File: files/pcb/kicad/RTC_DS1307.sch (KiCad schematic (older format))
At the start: 0 parts

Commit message: 回路図更新
温度湿度センサ
大気圧センサ
輝度センサ
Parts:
- added C?: 5.5V 0.1F, ~, symbol CP1
- added D?: DIODE, ~, symbol DIODE
- added IC?: DS1307, symbol IC_8PIN
- added R?: 100k, ~, symbol R
- added R?: 10k, ~, symbol R
- added X?: CRYSTAL, ~, symbol CRYSTAL
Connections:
- new net: IC?.1, X?.2
- new net: IC?.2, X?.1
- new net: C?.1, IC?.3, R?.2
- new net: D?.2 (K), R?.1
- new net +5V: D?.1 (A), IC?.8, R?.1
- new net CLKOUT: IC?.7, R?.2
- new net GND: C?.2, IC?.4
- new net SCL: IC?.6
- new net SDA: IC?.5
- no-connect marks 0 -> 1
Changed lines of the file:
@@
 $Descr A4 11693 8268
 encoding utf-8
-Sheet 1 12
+Sheet 10 12
 Title ""
 Date "23 aug 2014"
@@
 Comment4 ""
 $EndDescr
+Text HLabel 7200 4200 2    39   Input ~ 0
+SCL
+Text HLabel 7200 4300 2    39   Input ~ 0
+SDA
+Text HLabel 7200 4000 2    39   Input ~ 0
+CLKEN
+Text HLabel 7200 4100 2    39   Input ~ 0
+CLKOUT
+$Comp
+L IC_8PIN IC?
+U 1 1 53F95FB5
+P 6100 4150
+F 0 "IC?" H 6100 4400 39  0000 C CNN
+F 1 "DS1307" H 6100 4150 39  0000 C CNN
+F 2 "" H 6100 4050 60  0000 C CNN
+F 3 "" H 6100 4050 60  0000 C CNN
+	1    6100 4150
+	1    0    0    -1
+$EndComp
+$Comp
+L CRYSTAL X?
+U 1 1 53F95FD5
+P 5200 3850
+F 0 "X?" H 5200 4000 60  0000 C CNN
+F 1 "CRYSTAL" H 5200 3700 60  0000 C CNN
+F 2 "~" H 5200 3850 60  0000 C CNN
+F 3 "~" H 5200 3850 60  0000 C CNN
+	1    5200 3850
+	1    0    0    -1
+$EndComp
+$Comp
+L CP1 C?
+U 1 1 53F95FE8
+P 4550 4450
+F 0 "C?" H 4600 4550 50  0000 L CNN
+F 1 "5.5V 0.1F" H 4600 4350 50  0000 L CNN
+F 2 "~" H 4550 4450 60  0000 C CNN
+F 3 "~" H 4550 4450 60  0000 C CNN
+	1    4550 4450
+	1    0    0    -1
+$EndComp
+$Comp
+L DIODE D?
+U 1 1 53F95FF7
+P 4550 3400
+F 0 "D?" H 4550 3500 40  0000 C CNN
+F 1 "DIODE" H 4550 3300 40  0000 C CNN
+F 2 "~" H 4550 3400 60  0000 C CNN
+F 3 "~" H 4550 3400 60  0000 C CNN
+	1    4550 3400
+	0    1    1    0
+$EndComp
+$Comp
+L R R?
+U 1 1 53F96006
+P 4550 3900
+F 0 "R?" V 4630 3900 40  0000 C CNN
+F 1 "100k" V 4557 3901 40  0000 C CNN
+F 2 "~" V 4480 3900 30  0000 C CNN
+F 3 "~" H 4550 3900 30  0000 C CNN
+	1    4550 3900
+	1    0    0    -1
+$EndComp
+$Comp
+L +5V #PWR?
+U 1 1 53F9602E
+P 4550 3150
+F 0 "#PWR?" H 4550 3240 20  0001 C CNN
+F 1 "+5V" H 4550 3240 30  0000 C CNN
+F 2 "" H 4550 3150 60  0000 C CNN
+F 3 "" H 4550 3150 60  0000 C CNN
+	1    4550 3150
+	1    0    0    -1
+$EndComp
+$Comp
+L GND #PWR?
+U 1 1 53F96055
+P 4550 4750
+F 0 "#PWR?" H 4550 4750 30  0001 C CNN
+F 1 "GND" H 4550 4680 30  0001 C CNN
+F 2 "" H 4550 4750 60  0000 C CNN
+F 3 "" H 4550 4750 60  0000 C CNN
+	1    4550 4750
+	1    0    0    -1
+$EndComp
+Wire Wire Line
+	5650 4000 5500 4000
+Wire Wire Line
+	5650 4100 4900 4100
+Wire Wire Line
+	4900 4100 4900 3850
+Wire Wire Line
+	4550 3150 4550 3200
+Wire Wire Line
+	4550 3600 4550 3650
+Wire Wire Line
+	4550 4150 4550 4200
+Wire Wire Line
+	4550 4200 4550 4250
+Wire Wire Line
+	4550 4650 4550 4750
+Wire Wire Line
+	6700 4000 6550 4000
+Wire Wire Line
+	6700 3400 6700 4000
+Connection ~ 4550 4200
+Wire Wire Line
+	6550 4100 6950 4100
+Wire Wire Line
+	6950 4100 7200 4100
+Wire Wire Line
+	6950 4000 6950 4100
+$Comp
+L R R?
+U 1 1 53F960B9
+P 6950 3750
+F 0 "R?" V 7030 3750 40  0000 C CNN
+F 1 "10k" V 6957 3751 40  0000 C CNN
+F 2 "~" V 6880 3750 30  0000 C CNN
+F 3 "~" H 6950 3750 30  0000 C CNN
+	1    6950 3750
+	1    0    0    -1
+$EndComp
+Connection ~ 6950 4100
+Wire Wire Line
+	6550 4200 7200 4200
+Wire Wire Line
+	6550 4300 7200 4300
+NoConn ~ 7200 4000
+Wire Wire Line
+	5650 4200 4550 4200
+$Comp
+L +5V #PWR?
+U 1 1 53F961EF
+P 6700 3400
+F 0 "#PWR?" H 6700 3490 20  0001 C CNN
+F 1 "+5V" H 6700 3490 30  0000 C CNN
+F 2 "" H 6700 3400 60  0000 C CNN
+F 3 "" H 6700 3400 60  0000 C CNN
+	1    6700 3400
+	1    0    0    -1
+$EndComp
+$Comp
+L GND #PWR?
+U 1 1 53F961FF
+P 5500 4450
+F 0 "#PWR?" H 5500 4450 30  0001 C CNN
+F 1 "GND" H 5500 4380 30  0001 C CNN
+F 2 "" H 5500 4450 60  0000 C CNN
+F 3 "" H 5500 4450 60  0000 C CNN
+	1    5500 4450
+	1    0    0    -1
+$EndComp
+Wire Wire Line
+	5650 4300 5500 4300
+Wire Wire Line
+	5500 4300 5500 4450
+Wire Wire Line
+	6950 3400 6950 3500
+$Comp
+L +5V #PWR?
+U 1 1 53F96268
+P 6950 3400
+F 0 "#PWR?" H 6950 3490 20  0001 C CNN
+F 1 "+5V" H 6950 3490 30  0000 C CNN
+F 2 "" H 6950 3400 60  0000 C CNN
+F 3 "" H 6950 3400 60  0000 C CNN
+	1    6950 3400
+	1    0    0    -1
+$EndComp
+Wire Wire Line
+	5500 4000 5500 3850
 $EndSCHEMATC

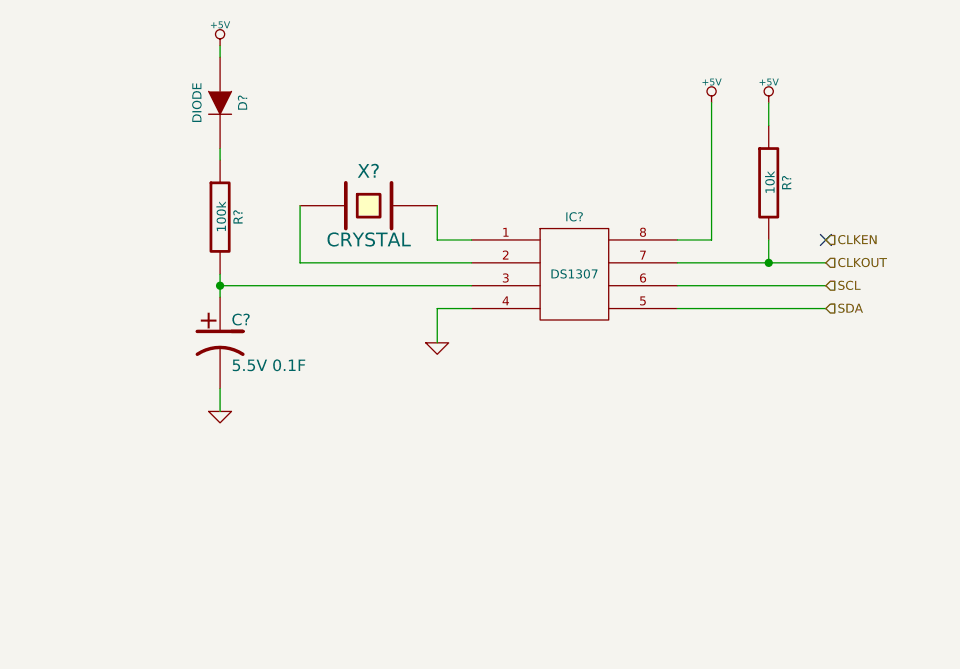
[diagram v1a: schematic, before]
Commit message: 回路図更新、DS1307対応
バスの接続が未
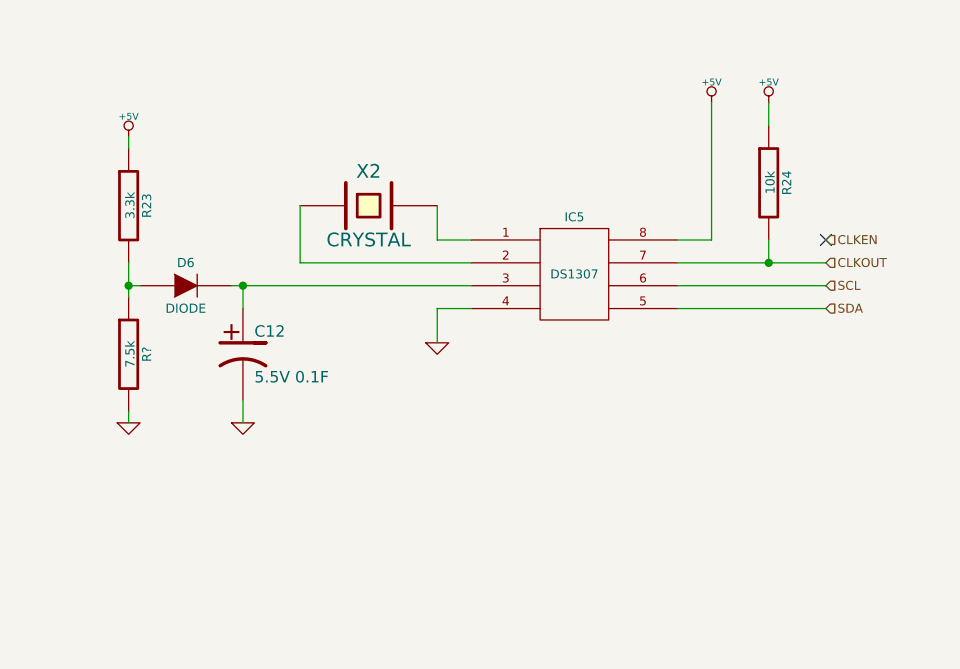
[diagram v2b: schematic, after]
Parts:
- added R?: 7.5k, ~, symbol R
- R23: renamed from R?; value 100k -> 3.3k
- gave numbers to parts that had none: 5
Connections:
- net +5V: now also R23.1; no longer D6.1 (A)
- net GND: now also R?.2
- net at C12.1, IC5.3: now also D6.2 (K); no longer R23.2
- new net: D6.1 (A), R23.2, R?.1
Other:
- moved on the sheet: C12, D6, R23
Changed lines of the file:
@@
 $Descr A4 11693 8268
 encoding utf-8
-Sheet 10 12
+Sheet 11 13
 Title ""
-Date "23 aug 2014"
+Date "24 aug 2014"
 Rev ""
 Comp ""
@@
 CLKOUT
 $Comp
-L IC_8PIN IC?
+L IC_8PIN IC5
 U 1 1 53F95FB5
 P 6100 4150
-F 0 "IC?" H 6100 4400 39  0000 C CNN
+F 0 "IC5" H 6100 4400 39  0000 C CNN
 F 1 "DS1307" H 6100 4150 39  0000 C CNN
 F 2 "" H 6100 4050 60  0000 C CNN
@@
 $EndComp
 $Comp
-L CRYSTAL X?
+L CRYSTAL X2
 U 1 1 53F95FD5
 P 5200 3850
-F 0 "X?" H 5200 4000 60  0000 C CNN
+F 0 "X2" H 5200 4000 60  0000 C CNN
 F 1 "CRYSTAL" H 5200 3700 60  0000 C CNN
 F 2 "~" H 5200 3850 60  0000 C CNN
@@
 $EndComp
 $Comp
-L CP1 C?
+L CP1 C12
 U 1 1 53F95FE8
-P 4550 4450
-F 0 "C?" H 4600 4550 50  0000 L CNN
-F 1 "5.5V 0.1F" H 4600 4350 50  0000 L CNN
-F 2 "~" H 4550 4450 60  0000 C CNN
-F 3 "~" H 4550 4450 60  0000 C CNN
-	1    4550 4450
-	1    0    0    -1
-$EndComp
-$Comp
-L DIODE D?
+P 4650 4500
+F 0 "C12" H 4700 4600 50  0000 L CNN
+F 1 "5.5V 0.1F" H 4700 4400 50  0000 L CNN
+F 2 "~" H 4650 4500 60  0000 C CNN
+F 3 "~" H 4650 4500 60  0000 C CNN
+	1    4650 4500
+	1    0    0    -1
+$EndComp
+$Comp
+L DIODE D6
 U 1 1 53F95FF7
-P 4550 3400
-F 0 "D?" H 4550 3500 40  0000 C CNN
-F 1 "DIODE" H 4550 3300 40  0000 C CNN
-F 2 "~" H 4550 3400 60  0000 C CNN
-F 3 "~" H 4550 3400 60  0000 C CNN
-	1    4550 3400
-	0    1    1    0
-$EndComp
-$Comp
-L R R?
+P 4400 4200
+F 0 "D6" H 4400 4300 40  0000 C CNN
+F 1 "DIODE" H 4400 4100 40  0000 C CNN
+F 2 "~" H 4400 4200 60  0000 C CNN
+F 3 "~" H 4400 4200 60  0000 C CNN
+	1    4400 4200
+	1    0    0    -1
+$EndComp
+$Comp
+L R R23
 U 1 1 53F96006
-P 4550 3900
-F 0 "R?" V 4630 3900 40  0000 C CNN
-F 1 "100k" V 4557 3901 40  0000 C CNN
-F 2 "~" V 4480 3900 30  0000 C CNN
-F 3 "~" H 4550 3900 30  0000 C CNN
-	1    4550 3900
-	1    0    0    -1
-$EndComp
-$Comp
-L +5V #PWR?
+P 4150 3850
+F 0 "R23" V 4230 3850 40  0000 C CNN
+F 1 "3.3k" V 4157 3851 40  0000 C CNN
+F 2 "~" V 4080 3850 30  0000 C CNN
+F 3 "~" H 4150 3850 30  0000 C CNN
+	1    4150 3850
+	1    0    0    -1
+$EndComp
+$Comp
+L +5V #PWR49
 U 1 1 53F9602E
-P 4550 3150
-F 0 "#PWR?" H 4550 3240 20  0001 C CNN
-F 1 "+5V" H 4550 3240 30  0000 C CNN
-F 2 "" H 4550 3150 60  0000 C CNN
-F 3 "" H 4550 3150 60  0000 C CNN
-	1    4550 3150
-	1    0    0    -1
-$EndComp
-$Comp
-L GND #PWR?
+P 4150 3550
+F 0 "#PWR49" H 4150 3640 20  0001 C CNN
+F 1 "+5V" H 4150 3640 30  0000 C CNN
+F 2 "" H 4150 3550 60  0000 C CNN
+F 3 "" H 4150 3550 60  0000 C CNN
+	1    4150 3550
+	1    0    0    -1
+$EndComp
+$Comp
+L GND #PWR50
 U 1 1 53F96055
-P 4550 4750
-F 0 "#PWR?" H 4550 4750 30  0001 C CNN
-F 1 "GND" H 4550 4680 30  0001 C CNN
-F 2 "" H 4550 4750 60  0000 C CNN
-F 3 "" H 4550 4750 60  0000 C CNN
-	1    4550 4750
+P 4150 4800
+F 0 "#PWR50" H 4150 4800 30  0001 C CNN
+F 1 "GND" H 4150 4730 30  0001 C CNN
+F 2 "" H 4150 4800 60  0000 C CNN
+F 3 "" H 4150 4800 60  0000 C CNN
+	1    4150 4800
 	1    0    0    -1
 $EndComp
@@
 	4900 4100 4900 3850
 Wire Wire Line
-	4550 3150 4550 3200
-Wire Wire Line
-	4550 3600 4550 3650
-Wire Wire Line
-	4550 4150 4550 4200
-Wire Wire Line
-	4550 4200 4550 4250
-Wire Wire Line
-	4550 4650 4550 4750
+	4150 3550 4150 3600
+Wire Wire Line
+	4150 4750 4150 4800
 Wire Wire Line
 	6700 4000 6550 4000
 Wire Wire Line
 	6700 3400 6700 4000
-Connection ~ 4550 4200
 Wire Wire Line
 	6550 4100 6950 4100
@@
 	6950 4000 6950 4100
 $Comp
-L R R?
+L R R24
 U 1 1 53F960B9
 P 6950 3750
-F 0 "R?" V 7030 3750 40  0000 C CNN
+F 0 "R24" V 7030 3750 40  0000 C CNN
 F 1 "10k" V 6957 3751 40  0000 C CNN
 F 2 "~" V 6880 3750 30  0000 C CNN
@@
 	6550 4300 7200 4300
 NoConn ~ 7200 4000
-Wire Wire Line
-	5650 4200 4550 4200
-$Comp
-L +5V #PWR?
+$Comp
+L +5V #PWR52
 U 1 1 53F961EF
 P 6700 3400
-F 0 "#PWR?" H 6700 3490 20  0001 C CNN
+F 0 "#PWR52" H 6700 3490 20  0001 C CNN
 F 1 "+5V" H 6700 3490 30  0000 C CNN
 F 2 "" H 6700 3400 60  0000 C CNN
@@
 $EndComp
 $Comp
-L GND #PWR?
+L GND #PWR51
 U 1 1 53F961FF
 P 5500 4450
-F 0 "#PWR?" H 5500 4450 30  0001 C CNN
+F 0 "#PWR51" H 5500 4450 30  0001 C CNN
 F 1 "GND" H 5500 4380 30  0001 C CNN
 F 2 "" H 5500 4450 60  0000 C CNN
@@
 	6950 3400 6950 3500
 $Comp
-L +5V #PWR?
+L +5V #PWR53
 U 1 1 53F96268
 P 6950 3400
-F 0 "#PWR?" H 6950 3490 20  0001 C CNN
+F 0 "#PWR53" H 6950 3490 20  0001 C CNN
 F 1 "+5V" H 6950 3490 30  0000 C CNN
 F 2 "" H 6950 3400 60  0000 C CNN
@@
 Wire Wire Line
 	5500 4000 5500 3850
+$Comp
+L R R?
+U 1 1 53FA233E
+P 4150 4500
+F 0 "R?" V 4230 4500 40  0000 C CNN
+F 1 "7.5k" V 4157 4501 40  0000 C CNN
+F 2 "~" V 4080 4500 30  0000 C CNN
+F 3 "~" H 4150 4500 30  0000 C CNN
+	1    4150 4500
+	1    0    0    -1
+$EndComp
+Wire Wire Line
+	4150 4100 4150 4200
+Wire Wire Line
+	4150 4200 4150 4250
+Wire Wire Line
+	4200 4200 4150 4200
+Connection ~ 4150 4200
+$Comp
+L GND #PWR?
+U 1 1 53FA2AE8
+P 4650 4800
+F 0 "#PWR?" H 4650 4800 30  0001 C CNN
+F 1 "GND" H 4650 4730 30  0001 C CNN
+F 2 "" H 4650 4800 60  0000 C CNN
+F 3 "" H 4650 4800 60  0000 C CNN
+	1    4650 4800
+	1    0    0    -1
+$EndComp
+Wire Wire Line
+	4650 4700 4650 4800
+Wire Wire Line
+	4650 4200 4650 4300
+Connection ~ 4650 4200
+Wire Wire Line
+	4600 4200 4650 4200
+Wire Wire Line
+	4650 4200 5650 4200
 $EndSCHEMATC

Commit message: 回路図ERC途中
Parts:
- gave numbers to parts that had none: 1
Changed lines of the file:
@@
 Sheet 11 13
 Title ""
-Date "24 aug 2014"
+Date "25 aug 2014"
 Rev ""
 Comp ""
@@
 $EndComp
 $Comp
-L +5V #PWR49
+L +5V #PWR051
 U 1 1 53F9602E
 P 4150 3550
-F 0 "#PWR49" H 4150 3640 20  0001 C CNN
+F 0 "#PWR051" H 4150 3640 20  0001 C CNN
 F 1 "+5V" H 4150 3640 30  0000 C CNN
 F 2 "" H 4150 3550 60  0000 C CNN
@@
 $EndComp
 $Comp
-L GND #PWR50
+L GND #PWR052
 U 1 1 53F96055
 P 4150 4800
-F 0 "#PWR50" H 4150 4800 30  0001 C CNN
+F 0 "#PWR052" H 4150 4800 30  0001 C CNN
 F 1 "GND" H 4150 4730 30  0001 C CNN
 F 2 "" H 4150 4800 60  0000 C CNN
@@
 	6700 3400 6700 4000
 Wire Wire Line
-	6550 4100 6950 4100
-Wire Wire Line
-	6950 4100 7200 4100
+	6550 4100 7200 4100
 Wire Wire Line
 	6950 4000 6950 4100
@@
 NoConn ~ 7200 4000
 $Comp
-L +5V #PWR52
+L +5V #PWR053
 U 1 1 53F961EF
 P 6700 3400
-F 0 "#PWR52" H 6700 3490 20  0001 C CNN
+F 0 "#PWR053" H 6700 3490 20  0001 C CNN
 F 1 "+5V" H 6700 3490 30  0000 C CNN
 F 2 "" H 6700 3400 60  0000 C CNN
@@
 $EndComp
 $Comp
-L GND #PWR51
+L GND #PWR054
 U 1 1 53F961FF
 P 5500 4450
-F 0 "#PWR51" H 5500 4450 30  0001 C CNN
+F 0 "#PWR054" H 5500 4450 30  0001 C CNN
 F 1 "GND" H 5500 4380 30  0001 C CNN
 F 2 "" H 5500 4450 60  0000 C CNN
@@
 	6950 3400 6950 3500
 $Comp
-L +5V #PWR53
+L +5V #PWR055
 U 1 1 53F96268
 P 6950 3400
-F 0 "#PWR53" H 6950 3490 20  0001 C CNN
+F 0 "#PWR055" H 6950 3490 20  0001 C CNN
 F 1 "+5V" H 6950 3490 30  0000 C CNN
 F 2 "" H 6950 3400 60  0000 C CNN
@@
 	5500 4000 5500 3850
 $Comp
-L R R?
+L R R29
 U 1 1 53FA233E
 P 4150 4500
-F 0 "R?" V 4230 4500 40  0000 C CNN
+F 0 "R29" V 4230 4500 40  0000 C CNN
 F 1 "7.5k" V 4157 4501 40  0000 C CNN
 F 2 "~" V 4080 4500 30  0000 C CNN
@@
 $EndComp
 Wire Wire Line
-	4150 4100 4150 4200
-Wire Wire Line
-	4150 4200 4150 4250
+	4150 4100 4150 4250
 Wire Wire Line
 	4200 4200 4150 4200
 Connection ~ 4150 4200
 $Comp
-L GND #PWR?
+L GND #PWR056
 U 1 1 53FA2AE8
 P 4650 4800
-F 0 "#PWR?" H 4650 4800 30  0001 C CNN
+F 0 "#PWR056" H 4650 4800 30  0001 C CNN
 F 1 "GND" H 4650 4730 30  0001 C CNN
 F 2 "" H 4650 4800 60  0000 C CNN
@@
 Connection ~ 4650 4200
 Wire Wire Line
-	4600 4200 4650 4200
-Wire Wire Line
-	4650 4200 5650 4200
+	4600 4200 5650 4200
 $EndSCHEMATC

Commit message: 回路図ERC完了
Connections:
- no-connect marks 1 -> 0
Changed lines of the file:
@@
 Sheet 11 13
 Title ""
-Date "25 aug 2014"
+Date "26 aug 2014"
 Rev ""
 Comp ""
@@
 Text HLabel 7200 4300 2    39   Input ~ 0
 SDA
-Text HLabel 7200 4000 2    39   Input ~ 0
-CLKEN
 Text HLabel 7200 4100 2    39   Input ~ 0
 CLKOUT
@@
 $EndComp
 $Comp
-L +5V #PWR051
+L +5V #PWR059
 U 1 1 53F9602E
 P 4150 3550
-F 0 "#PWR051" H 4150 3640 20  0001 C CNN
+F 0 "#PWR059" H 4150 3640 20  0001 C CNN
 F 1 "+5V" H 4150 3640 30  0000 C CNN
 F 2 "" H 4150 3550 60  0000 C CNN
@@
 $EndComp
 $Comp
-L GND #PWR052
+L GND #PWR060
 U 1 1 53F96055
 P 4150 4800
-F 0 "#PWR052" H 4150 4800 30  0001 C CNN
+F 0 "#PWR060" H 4150 4800 30  0001 C CNN
 F 1 "GND" H 4150 4730 30  0001 C CNN
 F 2 "" H 4150 4800 60  0000 C CNN
@@
 Wire Wire Line
 	6550 4300 7200 4300
-NoConn ~ 7200 4000
 $Comp
-L +5V #PWR053
+L +5V #PWR061
 U 1 1 53F961EF
 P 6700 3400
-F 0 "#PWR053" H 6700 3490 20  0001 C CNN
+F 0 "#PWR061" H 6700 3490 20  0001 C CNN
 F 1 "+5V" H 6700 3490 30  0000 C CNN
 F 2 "" H 6700 3400 60  0000 C CNN
@@
 $EndComp
 $Comp
-L GND #PWR054
+L GND #PWR062
 U 1 1 53F961FF
 P 5500 4450
-F 0 "#PWR054" H 5500 4450 30  0001 C CNN
+F 0 "#PWR062" H 5500 4450 30  0001 C CNN
 F 1 "GND" H 5500 4380 30  0001 C CNN
 F 2 "" H 5500 4450 60  0000 C CNN
@@
 	6950 3400 6950 3500
 $Comp
-L +5V #PWR055
+L +5V #PWR063
 U 1 1 53F96268
 P 6950 3400
-F 0 "#PWR055" H 6950 3490 20  0001 C CNN
+F 0 "#PWR063" H 6950 3490 20  0001 C CNN
 F 1 "+5V" H 6950 3490 30  0000 C CNN
 F 2 "" H 6950 3400 60  0000 C CNN
@@
 Connection ~ 4150 4200
 $Comp
-L GND #PWR056
+L GND #PWR064
 U 1 1 53FA2AE8
 P 4650 4800
-F 0 "#PWR056" H 4650 4800 30  0001 C CNN
+F 0 "#PWR064" H 4650 4800 30  0001 C CNN
 F 1 "GND" H 4650 4730 30  0001 C CNN
 F 2 "" H 4650 4800 60  0000 C CNN

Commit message: 部品リスト・パッケージライブラリを更新
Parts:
- renumbered C12 to C14, D6 to D5, IC5 to IC11, R23 to R27, R29 to R28, R24 to R29
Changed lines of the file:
@@
 CLKOUT
 $Comp
-L IC_8PIN IC5
+L IC_8PIN IC11
 U 1 1 53F95FB5
 P 6100 4150
-F 0 "IC5" H 6100 4400 39  0000 C CNN
+F 0 "IC11" H 6100 4400 39  0000 C CNN
 F 1 "DS1307" H 6100 4150 39  0000 C CNN
 F 2 "" H 6100 4050 60  0000 C CNN
@@
 $EndComp
 $Comp
-L CP1 C12
+L CP1 C14
 U 1 1 53F95FE8
 P 4650 4500
-F 0 "C12" H 4700 4600 50  0000 L CNN
+F 0 "C14" H 4700 4600 50  0000 L CNN
 F 1 "5.5V 0.1F" H 4700 4400 50  0000 L CNN
 F 2 "~" H 4650 4500 60  0000 C CNN
@@
 $EndComp
 $Comp
-L DIODE D6
+L DIODE D5
 U 1 1 53F95FF7
 P 4400 4200
-F 0 "D6" H 4400 4300 40  0000 C CNN
+F 0 "D5" H 4400 4300 40  0000 C CNN
 F 1 "DIODE" H 4400 4100 40  0000 C CNN
 F 2 "~" H 4400 4200 60  0000 C CNN
@@
 $EndComp
 $Comp
-L R R23
+L R R27
 U 1 1 53F96006
 P 4150 3850
-F 0 "R23" V 4230 3850 40  0000 C CNN
+F 0 "R27" V 4230 3850 40  0000 C CNN
 F 1 "3.3k" V 4157 3851 40  0000 C CNN
 F 2 "~" V 4080 3850 30  0000 C CNN
@@
 $EndComp
 $Comp
-L +5V #PWR059
+L +5V #PWR062
 U 1 1 53F9602E
 P 4150 3550
-F 0 "#PWR059" H 4150 3640 20  0001 C CNN
+F 0 "#PWR062" H 4150 3640 20  0001 C CNN
 F 1 "+5V" H 4150 3640 30  0000 C CNN
 F 2 "" H 4150 3550 60  0000 C CNN
@@
 $EndComp
 $Comp
-L GND #PWR060
+L GND #PWR063
 U 1 1 53F96055
 P 4150 4800
-F 0 "#PWR060" H 4150 4800 30  0001 C CNN
+F 0 "#PWR063" H 4150 4800 30  0001 C CNN
 F 1 "GND" H 4150 4730 30  0001 C CNN
 F 2 "" H 4150 4800 60  0000 C CNN
@@
 	6950 4000 6950 4100
 $Comp
-L R R24
+L R R29
 U 1 1 53F960B9
 P 6950 3750
-F 0 "R24" V 7030 3750 40  0000 C CNN
+F 0 "R29" V 7030 3750 40  0000 C CNN
 F 1 "10k" V 6957 3751 40  0000 C CNN
 F 2 "~" V 6880 3750 30  0000 C CNN
@@
 	6550 4300 7200 4300
 $Comp
-L +5V #PWR061
+L +5V #PWR064
 U 1 1 53F961EF
 P 6700 3400
-F 0 "#PWR061" H 6700 3490 20  0001 C CNN
+F 0 "#PWR064" H 6700 3490 20  0001 C CNN
 F 1 "+5V" H 6700 3490 30  0000 C CNN
 F 2 "" H 6700 3400 60  0000 C CNN
@@
 $EndComp
 $Comp
-L GND #PWR062
+L GND #PWR065
 U 1 1 53F961FF
 P 5500 4450
-F 0 "#PWR062" H 5500 4450 30  0001 C CNN
+F 0 "#PWR065" H 5500 4450 30  0001 C CNN
 F 1 "GND" H 5500 4380 30  0001 C CNN
 F 2 "" H 5500 4450 60  0000 C CNN
@@
 	6950 3400 6950 3500
 $Comp
-L +5V #PWR063
+L +5V #PWR066
 U 1 1 53F96268
 P 6950 3400
-F 0 "#PWR063" H 6950 3490 20  0001 C CNN
+F 0 "#PWR066" H 6950 3490 20  0001 C CNN
 F 1 "+5V" H 6950 3490 30  0000 C CNN
 F 2 "" H 6950 3400 60  0000 C CNN
@@
 	5500 4000 5500 3850
 $Comp
-L R R29
+L R R28
 U 1 1 53FA233E
 P 4150 4500
-F 0 "R29" V 4230 4500 40  0000 C CNN
+F 0 "R28" V 4230 4500 40  0000 C CNN
 F 1 "7.5k" V 4157 4501 40  0000 C CNN
 F 2 "~" V 4080 4500 30  0000 C CNN
@@
 Connection ~ 4150 4200
 $Comp
-L GND #PWR064
+L GND #PWR067
 U 1 1 53FA2AE8
 P 4650 4800
-F 0 "#PWR064" H 4650 4800 30  0001 C CNN
+F 0 "#PWR067" H 4650 4800 30  0001 C CNN
 F 1 "GND" H 4650 4730 30  0001 C CNN
 F 2 "" H 4650 4800 60  0000 C CNN

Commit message: 部品リスト完了、PCBに部品を配置
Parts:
- added C18: 0.1u, ~, symbol C
- X2: value CRYSTAL -> 32.768kHz
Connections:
- net +5V: now also C18.1
- net GND: now also C18.2
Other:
- moved on the sheet: R29
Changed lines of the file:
@@
 Sheet 11 13
 Title ""
-Date "26 aug 2014"
+Date "28 aug 2014"
 Rev ""
 Comp ""
@@
 Comment4 ""
 $EndDescr
-Text HLabel 7200 4200 2    39   Input ~ 0
+Text HLabel 7400 4200 2    39   Input ~ 0
 SCL
-Text HLabel 7200 4300 2    39   Input ~ 0
+Text HLabel 7400 4300 2    39   Input ~ 0
 SDA
-Text HLabel 7200 4100 2    39   Input ~ 0
+Text HLabel 7400 4100 2    39   Input ~ 0
 CLKOUT
 $Comp
@@
 P 5200 3850
 F 0 "X2" H 5200 4000 60  0000 C CNN
-F 1 "CRYSTAL" H 5200 3700 60  0000 C CNN
+F 1 "32.768kHz" H 5200 3700 60  0000 C CNN
 F 2 "~" H 5200 3850 60  0000 C CNN
 F 3 "~" H 5200 3850 60  0000 C CNN
@@
 	6700 3400 6700 4000
 Wire Wire Line
-	6550 4100 7200 4100
-Wire Wire Line
-	6950 4000 6950 4100
+	6550 4100 7400 4100
+Wire Wire Line
+	7150 4000 7150 4100
 $Comp
 L R R29
 U 1 1 53F960B9
-P 6950 3750
-F 0 "R29" V 7030 3750 40  0000 C CNN
-F 1 "10k" V 6957 3751 40  0000 C CNN
-F 2 "~" V 6880 3750 30  0000 C CNN
-F 3 "~" H 6950 3750 30  0000 C CNN
-	1    6950 3750
-	1    0    0    -1
-$EndComp
-Connection ~ 6950 4100
-Wire Wire Line
-	6550 4200 7200 4200
-Wire Wire Line
-	6550 4300 7200 4300
+P 7150 3750
+F 0 "R29" V 7230 3750 40  0000 C CNN
+F 1 "10k" V 7157 3751 40  0000 C CNN
+F 2 "~" V 7080 3750 30  0000 C CNN
+F 3 "~" H 7150 3750 30  0000 C CNN
+	1    7150 3750
+	1    0    0    -1
+$EndComp
+Connection ~ 7150 4100
+Wire Wire Line
+	6550 4200 7400 4200
+Wire Wire Line
+	6550 4300 7400 4300
 $Comp
 L +5V #PWR064
@@
 	5500 4300 5500 4450
 Wire Wire Line
-	6950 3400 6950 3500
+	7150 3400 7150 3500
 $Comp
 L +5V #PWR066
 U 1 1 53F96268
-P 6950 3400
-F 0 "#PWR066" H 6950 3490 20  0001 C CNN
-F 1 "+5V" H 6950 3490 30  0000 C CNN
-F 2 "" H 6950 3400 60  0000 C CNN
-F 3 "" H 6950 3400 60  0000 C CNN
-	1    6950 3400
+P 7150 3400
+F 0 "#PWR066" H 7150 3490 20  0001 C CNN
+F 1 "+5V" H 7150 3490 30  0000 C CNN
+F 2 "" H 7150 3400 60  0000 C CNN
+F 3 "" H 7150 3400 60  0000 C CNN
+	1    7150 3400
 	1    0    0    -1
 $EndComp
@@
 Wire Wire Line
 	4600 4200 5650 4200
+$Comp
+L C C18
+U 1 1 53FF68E6
+P 6850 3750
+F 0 "C18" H 6850 3850 40  0000 L CNN
+F 1 "0.1u" H 6856 3665 40  0000 L CNN
+F 2 "~" H 6888 3600 30  0000 C CNN
+F 3 "~" H 6850 3750 60  0000 C CNN
+	1    6850 3750
+	1    0    0    -1
+$EndComp
+$Comp
+L GND #PWR068
+U 1 1 53FF68F8
+P 6850 4000
+F 0 "#PWR068" H 6850 4000 30  0001 C CNN
+F 1 "GND" H 6850 3930 30  0001 C CNN
+F 2 "" H 6850 4000 60  0000 C CNN
+F 3 "" H 6850 4000 60  0000 C CNN
+	1    6850 4000
+	1    0    0    -1
+$EndComp
+Wire Wire Line
+	6850 4000 6850 3950
+Wire Wire Line
+	6850 3550 6850 3500
+Wire Wire Line
+	6850 3500 6700 3500
+Connection ~ 6700 3500
 $EndSCHEMATC
